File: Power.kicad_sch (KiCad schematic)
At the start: 6 parts, among them J3 Conn_01x02, Q1 Q_PMOS_GDS

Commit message: inital sch
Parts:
- removed R11: 49.9k, Resistor_SMD:R_0805_2012Metric, symbol Device:R_US
- added IC1: 1769205241, Active-PrechargeLib:1769205241, symbol DCDC-isolator:1769205241
- added ISO_PWR_TP1: TestPoint, utsvt-special:TestPoint_HEX_3mmID, symbol Connector:TestPoint
- added R1: 49.9k, Resistor_SMD:R_0805_2012Metric, symbol Device:R_US
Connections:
- net HVGND: now also IC1.4 (-VOUT)
- net ISO_PWR: now also IC1.5 (+VOUT), ISO_PWR_TP1.1
- net LV+: now also IC1.2 (+VIN)
- net LVGND: now also IC1.1 (-VIN), R1.1
- net at D1.2 (A), Q1.1 (G): now also R1.2
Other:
- removed sheet ActivePrecharge
- removed sheet CAN
- removed sheet ContactorDriver
- removed sheet PowerMisc
- moved on the sheet: 12V_TP1, D1, J3, LVGND_TP1, Q1

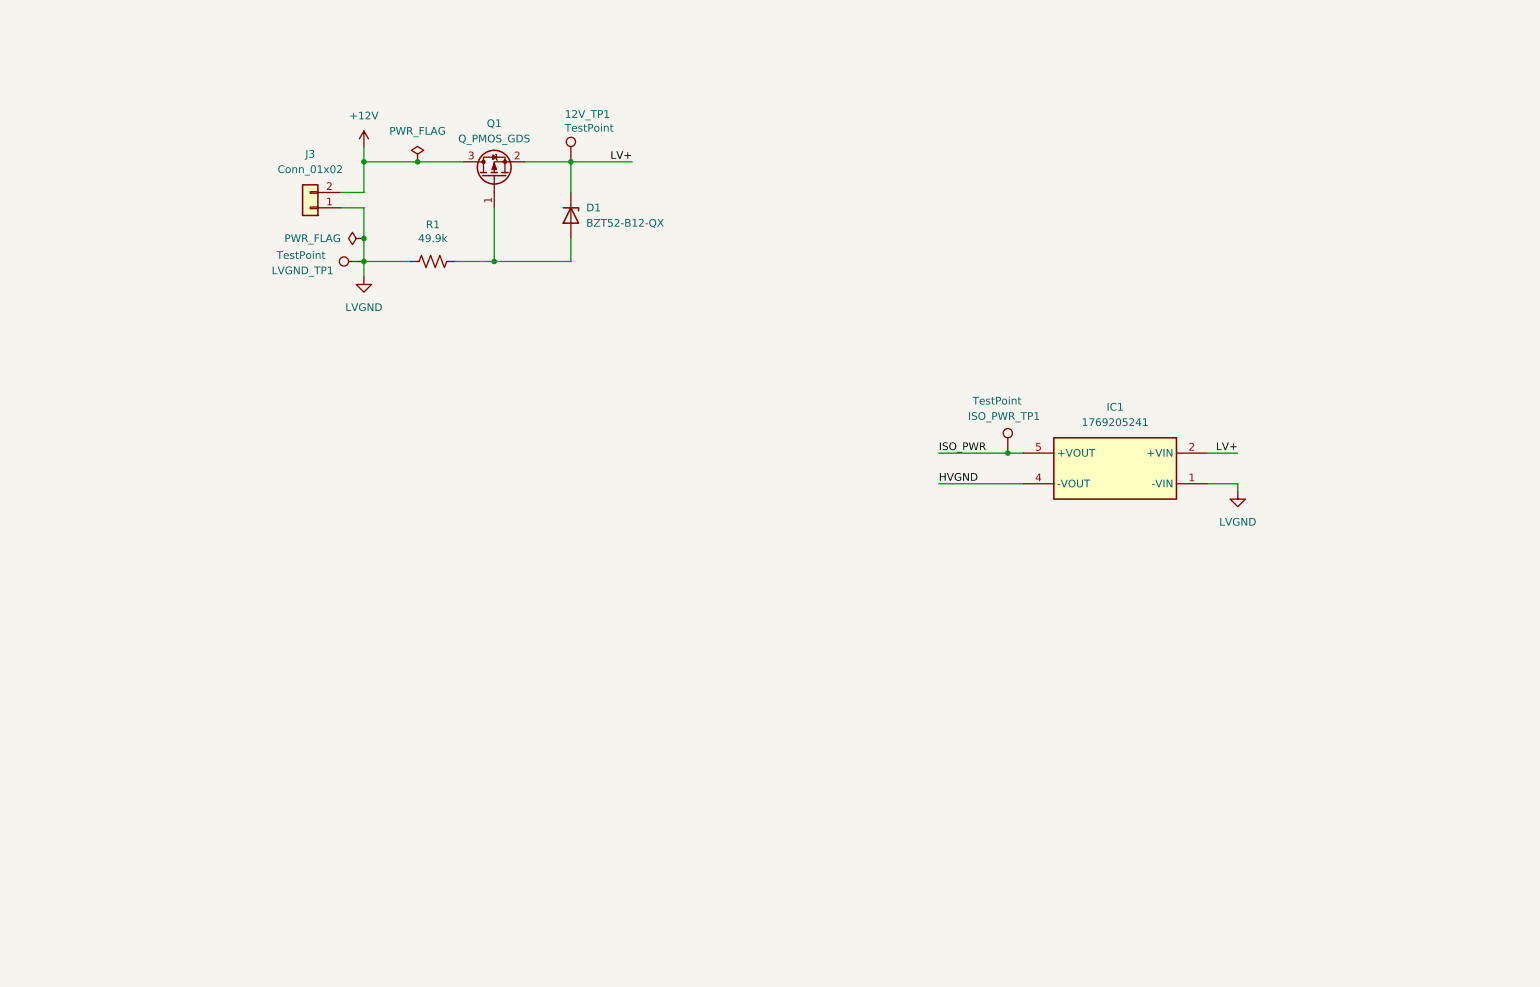
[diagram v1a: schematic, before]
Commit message: changed rpp ic
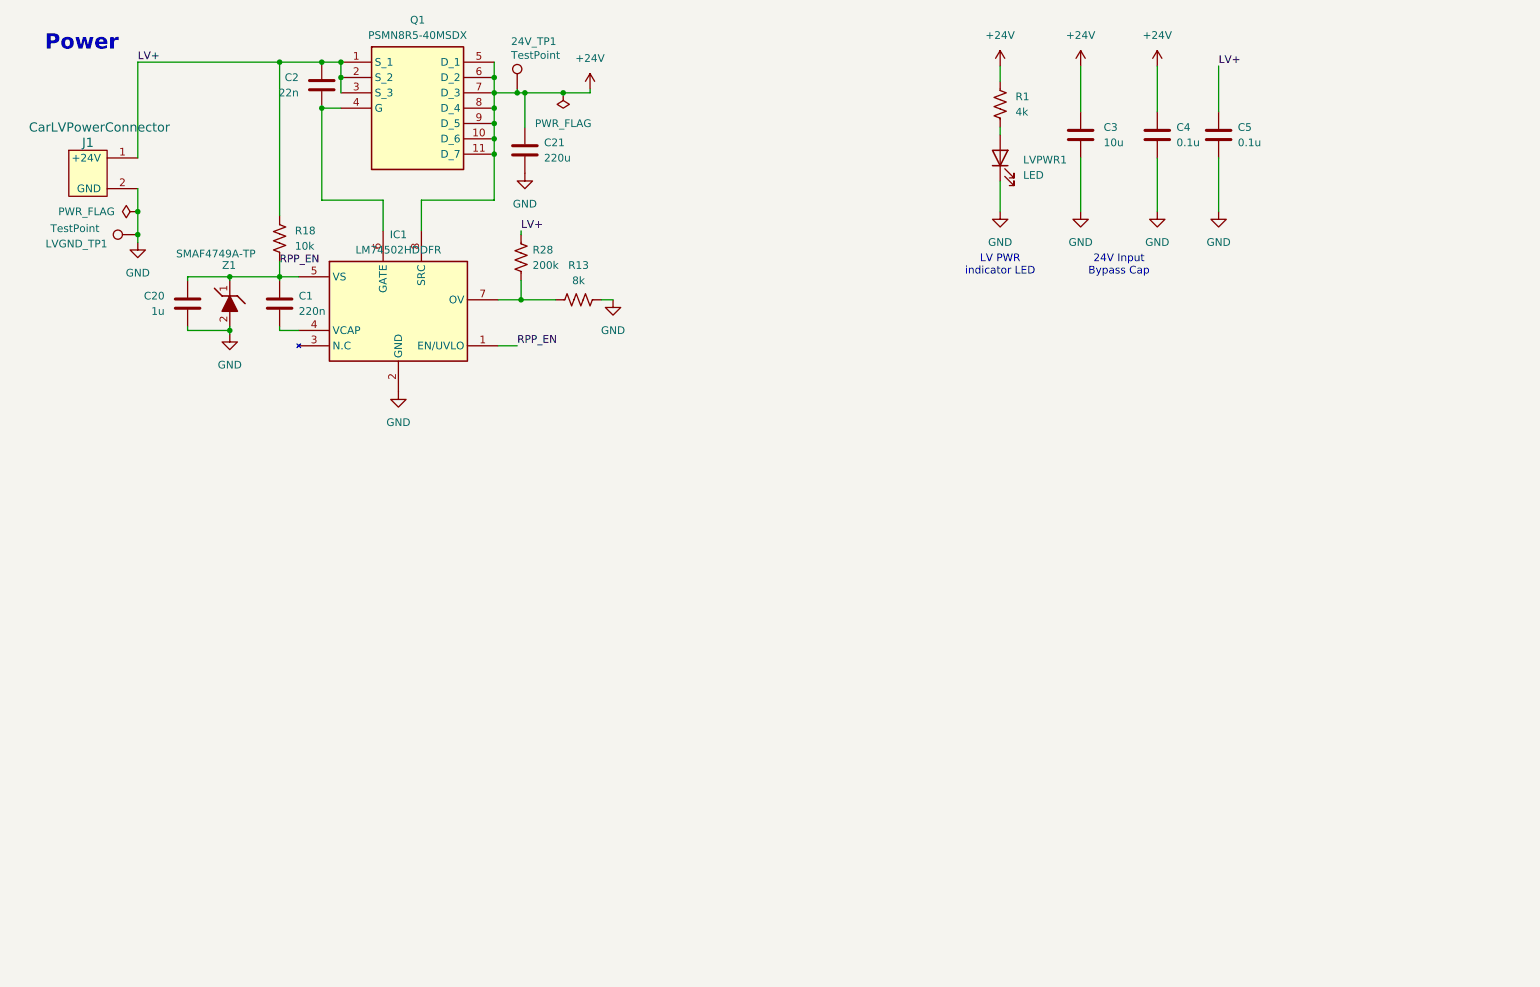
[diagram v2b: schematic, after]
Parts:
- removed D1: BZT52-B12-QX, Active-PrechargeLib:BZT52B12QX, symbol Device:D_Zener
- removed IC1: 1769205241, Active-PrechargeLib:1769205241, symbol DCDC-isolator:1769205241
- removed ISO_PWR_TP1: TestPoint, utsvt-special:TestPoint_HEX_3mmID, symbol Connector:TestPoint
- removed J3: Conn_01x02, utsvt-conn:Molex_MicroFit3.0_1x2xP3.00mm_PolarizingPeg_Vertical, symbol Connector_Generic:Conn_01x02
- removed Q1: Q_PMOS_GDS, Package_TO_SOT_SMD:SOT-23-3, symbol Device:Q_PMOS_GDS
- added C1: 220n, Capacitor_SMD:C_0603_1608Metric, symbol Device:C
- added C2: 22n, Capacitor_SMD:C_0603_1608Metric, symbol Device:C
- added C20: 1u, Capacitor_SMD:C_0603_1608Metric, symbol Device:C
- added C21: 220u, symbol Device:C
- added C3: 10u, Capacitor_SMD:C_0603_1608Metric, symbol Device:C
- added C4, C5: 0.1u, Capacitor_SMD:C_0603_1608Metric, symbol Device:C
- added IC1: LM74502HDDFR, SOT65P280X110-8N, symbol UTSVT_ICs:LM74502HDDFR
- added J1: CarLVPowerConnector, symbol UTSVT_Connectors:CarLVPowerConnector
- added LVPWR1: LED, LED_SMD:LED_0603_1608Metric, symbol Device:LED
- added Q1: PSMN8R5-40MSDX, PSMN8R5-40MSDX, symbol UTSVT_Power:PSMN8R5-40MSDX
- added R13: 8k, symbol Device:R_US
- added R18: 10k, symbol Device:R_US
- added R28: 200k, symbol Device:R_US
- added Z1: SMAF4749A-TP, SODFL5026X125N, symbol UTSVT_Power:SMAF4749A-TP
- 24V_TP1: renamed from 12V_TP1; footprint utsvt-special:TestPoint_HEX_3mmID -> UTSVT_Special:TestPoint_HEX_3mmID
- LVGND_TP1: footprint utsvt-special:TestPoint_HEX_3mmID -> UTSVT_Special:TestPoint_HEX_3mmID
- R1: value 49.9k -> 4k; footprint Resistor_SMD:R_0805_2012Metric -> Resistor_SMD:R_0603_1608Metric
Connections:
- net LV+: now also C2.2, C5.1, J1.1 (+24V), Q1.1 (S_1), Q1.2 (S_2), Q1.3 (S_3), R18.1, R28.1; no longer 24V_TP1.1
- net at R1.2: now also LVPWR1.2 (A)
- net LVGND renamed +24V
- net +24V: now also 24V_TP1.1, C21.1, C3.1, C4.1, IC1.8 (SRC), Q1.10 (D_6), Q1.11 (D_7), Q1.5 (D_1), Q1.6 (D_2), Q1.7 (D_3), Q1.8 (D_4), Q1.9 (D_5); no longer LVGND_TP1.1
- new net: C1.2, IC1.4 (VCAP)
- new net: C2.1, IC1.6 (GATE), Q1.4 (G)
- new net: IC1.7 (OV), R13.1, R28.2
- new net GND: C20.1, C21.2, C3.2, C4.2, C5.2, IC1.2 (GND), J1.2 (GND), LVGND_TP1.1, LVPWR1.1 (K), R13.2, Z1.2 (A)
- new net RPP_EN: C1.1, C20.2, IC1.1 (EN/UVLO), IC1.5 (VS), R18.2, Z1.1 (K)
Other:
- note added: "24V Input Bypass Cap"
- note added: "LV PWR indicator LED"
- note added: "Power"
- moved on the sheet: 24V_TP1, LVGND_TP1

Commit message: as;ldfkjasdl;f
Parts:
- added J3: Conn_01x02, UTSVT_Connectors:Molex_Nano-Fit_105309-xx02_1x02_P2.50mm_Vertical, symbol Connector_Generic:Conn_01x02
- C21: footprint (none) -> Capacitor_SMD:C_0603_1608Metric
- IC1: footprint SOT65P280X110-8N -> UTSVT_Power:SOT65P280X110-8N
- J1: footprint (none) -> UTSVT_Connectors:Molex_Nano-Fit_105309-xx02_1x02_P2.50mm_Vertical
- Q1: footprint PSMN8R5-40MSDX -> UTSVT_Power:PSMN8R5-40MSDX
- R13, R18, R28: footprint (none) -> Resistor_SMD:R_0603_1608Metric
- Z1: footprint SODFL5026X125N -> UTSVT_Passives:SODFL5026X125N
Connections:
- net GND: now also J3.1 (Pin_1)
- new net +3V3: J3.2 (Pin_2)
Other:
- note added: "3v3 injector"
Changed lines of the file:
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@@
 	(generator_version "9.0")
 	(paper "A4")
+	(text "3v3 injector"
+		(exclude_from_sim no)
+		(at 38.735 93.98 0)
+		(effects
+			(font
+				(size 1.27 1.27)
+			)
+		)
+	)
 	(text "LV PWR \nindicator LED"
 		(exclude_from_sim no)
@@
 	(wire
 		(pts
+			(xy 43.815 106.68) (xy 50.165 106.68)
+		)
+		(stroke
+			(width 0)
+			(type default)
+		)
+	)
+	(wire
+		(pts
 			(xy 106.68 33.02) (xy 106.68 35.56)
 		)
@@
 	(wire
 		(pts
+			(xy 43.815 104.14) (xy 50.165 104.14)
+		)
+		(stroke
+			(width 0)
+			(type default)
+		)
+	)
+	(wire
+		(pts
 			(xy 78.105 40.64) (xy 81.28 40.64)
 		)
@@
 	)
 	(symbol
+		(lib_id "power:GND")
+		(at 50.165 106.68 0)
+		(unit 1)
+		(exclude_from_sim no)
+		(in_bom yes)
+		(on_board yes)
+		(dnp no)
+		(fields_autoplaced yes)
+		(property "Reference" "#PWR045"
+			(at 50.165 113.03 0)
+			(effects
+				(font
+					(size 1.27 1.27)
+				)
+				(hide yes)
+			)
+		)
+		(property "Value" "GND"
+			(at 50.165 111.76 0)
+			(effects
+				(font
+					(size 1.27 1.27)
+				)
+			)
+		)
+		(property "Footprint" ""
+			(at 50.165 106.68 0)
+			(effects
+				(font
+					(size 1.27 1.27)
+				)
+				(hide yes)
+			)
+		)
+		(property "Datasheet" ""
+			(at 50.165 106.68 0)
+			(effects
+				(font
+					(size 1.27 1.27)
+				)
+				(hide yes)
+			)
+		)
+		(property "Description" "Power symbol creates a global label with name \"GND\" , ground"
+			(at 50.165 106.68 0)
+			(effects
+				(font
+					(size 1.27 1.27)
+				)
+				(hide yes)
+			)
+		)
+		(pin "1"
+		)
+		(instances
+			(project "VehicleControlUnit"
+				(path "/795c8e51-3ded-4d21-b864-aaff31c5def7/5469fc22-573e-4402-96df-d8b4b5bb4d29"
+					(reference "#PWR045")
+					(unit 1)
+				)
+			)
+		)
+	)
+	(symbol
 		(lib_id "power:+12V")
 		(at 216.535 33.655 0)
@@
 			)
 		)
-		(property "Footprint" ""
+		(property "Footprint" "Resistor_SMD:R_0603_1608Metric"
 			(at 72.136 62.484 90)
 			(effects
@@
 			)
 		)
-		(property "Footprint" "PSMN8R5-40MSDX"
+		(property "Footprint" "UTSVT_Power:PSMN8R5-40MSDX"
 			(at 102.87 127.94 0)
 			(effects
@@
 	)
 	(symbol
+		(lib_id "power:+3V3")
+		(at 50.165 104.14 0)
+		(unit 1)
+		(exclude_from_sim no)
+		(in_bom yes)
+		(on_board yes)
+		(dnp no)
+		(fields_autoplaced yes)
+		(property "Reference" "#PWR041"
+			(at 50.165 107.95 0)
+			(effects
+				(font
+					(size 1.27 1.27)
+				)
+				(hide yes)
+			)
+		)
+		(property "Value" "+3V3"
+			(at 50.165 99.06 0)
+			(effects
+				(font
+					(size 1.27 1.27)
+				)
+			)
+		)
+		(property "Footprint" ""
+			(at 50.165 104.14 0)
+			(effects
+				(font
+					(size 1.27 1.27)
+				)
+				(hide yes)
+			)
+		)
+		(property "Datasheet" ""
+			(at 50.165 104.14 0)
+			(effects
+				(font
+					(size 1.27 1.27)
+				)
+				(hide yes)
+			)
+		)
+		(property "Description" "Power symbol creates a global label with name \"+3V3\""
+			(at 50.165 104.14 0)
+			(effects
+				(font
+					(size 1.27 1.27)
+				)
+				(hide yes)
+			)
+		)
+		(pin "1"
+		)
+		(instances
+			(project "VehicleControlUnit"
+				(path "/795c8e51-3ded-4d21-b864-aaff31c5def7/5469fc22-573e-4402-96df-d8b4b5bb4d29"
+					(reference "#PWR041")
+					(unit 1)
+				)
+			)
+		)
+	)
+	(symbol
 		(lib_id "power:GND")
 		(at 203.835 57.785 0)
@@
 	)
 	(symbol
+		(lib_id "Connector_Generic:Conn_01x02")
+		(at 38.735 106.68 180)
+		(unit 1)
+		(exclude_from_sim no)
+		(in_bom yes)
+		(on_board yes)
+		(dnp no)
+		(fields_autoplaced yes)
+		(property "Reference" "J3"
+			(at 38.735 97.79 0)
+			(effects
+				(font
+					(size 1.27 1.27)
+				)
+			)
+		)
+		(property "Value" "Conn_01x02"
+			(at 38.735 100.33 0)
+			(effects
+				(font
+					(size 1.27 1.27)
+				)
+			)
+		)
+		(property "Footprint" "UTSVT_Connectors:Molex_Nano-Fit_105309-xx02_1x02_P2.50mm_Vertical"
+			(at 38.735 106.68 0)
+			(effects
+				(font
+					(size 1.27 1.27)
+				)
+				(hide yes)
+			)
+		)
+		(property "Datasheet" "~"
+			(at 38.735 106.68 0)
+			(effects
+				(font
+					(size 1.27 1.27)
+				)
+				(hide yes)
+			)
+		)
+		(property "Description" "Generic connector, single row, 01x02, script generated (kicad-library-utils/schlib/autogen/connector/)"
+			(at 38.735 106.68 0)
+			(effects
+				(font
+					(size 1.27 1.27)
+				)
+				(hide yes)
+			)
+		)
+		(pin "2"
+		)
+		(pin "1"
+		)
+		(instances
+			(project ""
+				(path "/795c8e51-3ded-4d21-b864-aaff31c5def7/5469fc22-573e-4402-96df-d8b4b5bb4d29"
+					(reference "J3")
+					(unit 1)
+				)
+			)
+		)
+	)
+	(symbol
 		(lib_id "UTSVT_ICs:LM74502HDDFR")
 		(at 74.295 68.58 0)
@@
 			)
 		)
-		(property "Footprint" "SOT65P280X110-8N"
+		(property "Footprint" "UTSVT_Power:SOT65P280X110-8N"
 			(at 103.505 163.5 0)
 			(effects
@@
 			)
 		)
-		(property "Footprint" "SODFL5026X125N"
+		(property "Footprint" "UTSVT_Passives:SODFL5026X125N"
 			(at -30.785 76.835 0)
 			(effects
@@
 			)
 		)
-		(property "Footprint" ""
+		(property "Footprint" "Capacitor_SMD:C_0603_1608Metric"
 			(at 112.7252 51.435 0)
 			(effects
@@
 			)
 		)
-		(property "Footprint" ""
+		(property "Footprint" "Resistor_SMD:R_0603_1608Metric"
 			(at 120.904 71.374 90)
 			(effects
@@
 			)
 		)
-		(property "Footprint" ""
+		(property "Footprint" "Resistor_SMD:R_0603_1608Metric"
 			(at 112.141 65.659 90)
 			(effects
@@
 			)
 		)
-		(property "Footprint" ""
+		(property "Footprint" "UTSVT_Connectors:Molex_Nano-Fit_105309-xx02_1x02_P2.50mm_Vertical"
 			(at 40.005 51.435 0)
 			(effects

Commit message: maybe final revA revision
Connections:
- net +3V3 renamed 3V3_LSOM

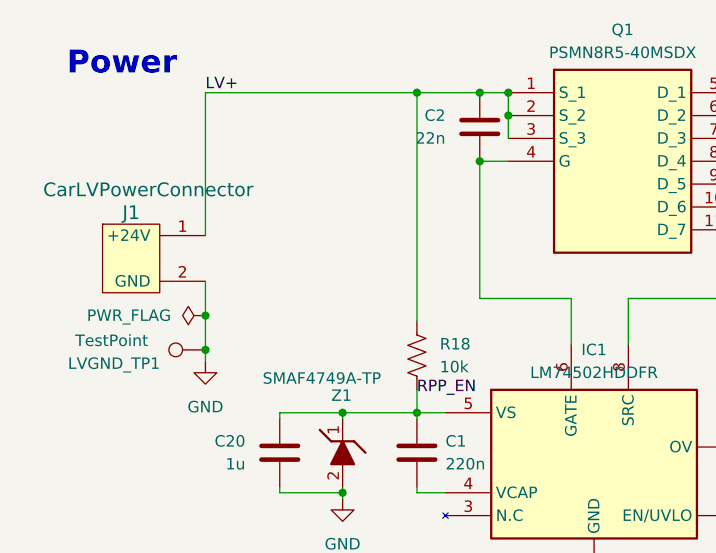
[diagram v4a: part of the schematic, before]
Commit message: small zener diode change
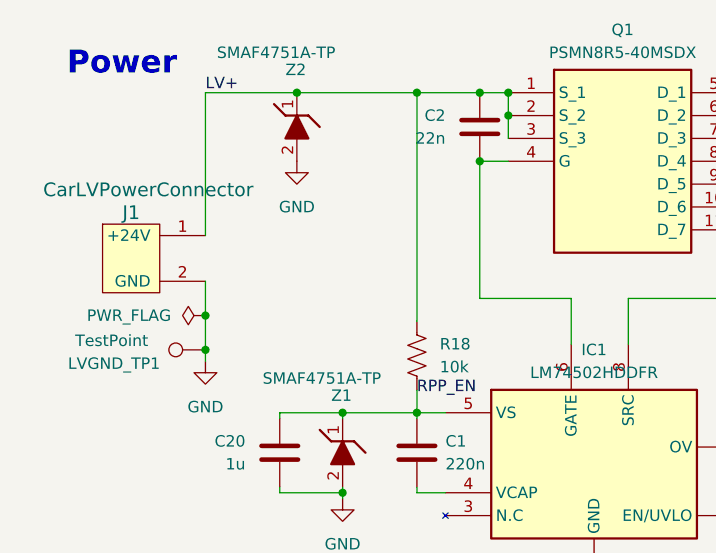
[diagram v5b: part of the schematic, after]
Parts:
- added Z2: SMAF4751A-TP, UTSVT_Passives:SODFL5026X125N, symbol UTSVT_Power:SMAF4749A-TP
- Z1: value SMAF4749A-TP -> SMAF4751A-TP
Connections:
- net GND: now also Z2.2 (A)
- net LV+: now also Z2.1 (K)
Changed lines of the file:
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@@
 	)
 	(junction
+		(at 57.785 33.02)
+		(diameter 0)
+		(color 0 0 0 0)
+	)
+	(junction
 		(at 62.865 77.47)
 		(diameter 0)
@@
 	(wire
 		(pts
-			(xy 47.625 33.02) (xy 71.12 33.02)
+			(xy 47.625 33.02) (xy 57.785 33.02)
 		)
 		(stroke
@@
 	(wire
 		(pts
+			(xy 57.785 33.02) (xy 71.12 33.02)
+		)
+		(stroke
+			(width 0)
+			(type default)
+		)
+	)
+	(wire
+		(pts
 			(xy 111.76 38.1) (xy 118.11 38.1)
 		)
@@
 	(symbol
 		(lib_id "UTSVT_Power:SMAF4749A-TP")
+		(at 57.785 30.48 270)
+		(unit 1)
+		(exclude_from_sim no)
+		(in_bom yes)
+		(on_board yes)
+		(dnp no)
+		(property "Reference" "Z2"
+			(at 56.515 30.48 90)
+			(effects
+				(font
+					(size 1.27 1.27)
+				)
+				(justify left)
+			)
+		)
+		(property "Value" "SMAF4751A-TP"
+			(at 48.895 28.575 90)
+			(effects
+				(font
+					(size 1.27 1.27)
+				)
+				(justify left)
+			)
+		)
+		(property "Footprint" "UTSVT_Passives:SODFL5026X125N"
+			(at -35.865 40.64 0)
+			(effects
+				(font
+					(size 1.27 1.27)
+				)
+				(justify left top)
+				(hide yes)
+			)
+		)
+		(property "Datasheet" "https://www.mccsemi.com/pdf/Products/SMAF4735A_SMAF4764A(DO-221AC).pdf"
+			(at -135.865 40.64 0)
+			(effects
+				(font
+					(size 1.27 1.27)
+				)
+				(justify left top)
+				(hide yes)
+			)
+		)
+		(property "Description" "1.0 Watt Zener Diodes 6.2V to 100V"
+			(at 57.785 30.48 0)
+			(effects
+				(font
+					(size 1.27 1.27)
+				)
+				(hide yes)
+			)
+		)
+		(property "Height" "1.25"
+			(at -335.865 40.64 0)
+			(effects
+				(font
+					(size 1.27 1.27)
+				)
+				(justify left top)
+				(hide yes)
+			)
+		)
+		(property "Mouser Part Number" "833-SMAF4749A-TP"
+			(at -435.865 40.64 0)
+			(effects
+				(font
+					(size 1.27 1.27)
+				)
+				(justify left top)
+				(hide yes)
+			)
+		)
+		(property "Mouser Price/Stock" "https://www.mouser.co.uk/ProductDetail/Micro-Commercial-Components-MCC/SMAF4749A-TP?qs=%252BXxaIXUDbq1bdSZ3Ebik%2FA%3D%3D"
+			(at -535.865 40.64 0)
+			(effects
+				(font
+					(size 1.27 1.27)
+				)
+				(justify left top)
+				(hide yes)
+			)
+		)
+		(property "Manufacturer_Name" "MCC"
+			(at -635.865 40.64 0)
+			(effects
+				(font
+					(size 1.27 1.27)
+				)
+				(justify left top)
+				(hide yes)
+			)
+		)
+		(property "Manufacturer_Part_Number" "SMAF4749A-TP"
+			(at -735.865 40.64 0)
+			(effects
+				(font
+					(size 1.27 1.27)
+				)
+				(justify left top)
+				(hide yes)
+			)
+		)
+		(pin "1"
+		)
+		(pin "2"
+		)
+		(instances
+			(project "VehicleControlUnit"
+				(path "/795c8e51-3ded-4d21-b864-aaff31c5def7/5469fc22-573e-4402-96df-d8b4b5bb4d29"
+					(reference "Z2")
+					(unit 1)
+				)
+			)
+		)
+	)
+	(symbol
+		(lib_id "UTSVT_Power:SMAF4749A-TP")
 		(at 62.865 66.675 270)
 		(unit 1)
@@
 			)
 		)
-		(property "Value" "SMAF4749A-TP"
+		(property "Value" "SMAF4751A-TP"
 			(at 53.975 64.77 90)
 			(effects
@@
 					(unit 1)
 				)
+			)
+		)
+	)
+	(symbol
+		(lib_id "power:GND")
+		(at 57.785 40.64 0)
+		(unit 1)
+		(exclude_from_sim no)
+		(in_bom yes)
+		(on_board yes)
+		(dnp no)
+		(fields_autoplaced yes)
+		(property "Reference" "#PWR076"
+			(at 57.785 46.99 0)
+			(effects
+				(font
+					(size 1.27 1.27)
+				)
+				(hide yes)
+			)
+		)
+		(property "Value" "GND"
+			(at 57.785 45.72 0)
+			(effects
+				(font
+					(size 1.27 1.27)
+				)
+			)
+		)
+		(property "Footprint" ""
+			(at 57.785 40.64 0)
+			(effects
+				(font
+					(size 1.27 1.27)
+				)
+				(hide yes)
+			)
+		)
+		(property "Datasheet" ""
+			(at 57.785 40.64 0)
+			(effects
+				(font
+					(size 1.27 1.27)
+				)
+				(hide yes)
+			)
+		)
+		(property "Description" "Power symbol creates a global label with name \"GND\" , ground"
+			(at 57.785 40.64 0)
+			(effects
+				(font
+					(size 1.27 1.27)
+				)
+				(hide yes)
+			)
+		)
+		(pin "1"
+		)
+		(instances
+			(project "VehicleControlUnit"
+				(path "/795c8e51-3ded-4d21-b864-aaff31c5def7/5469fc22-573e-4402-96df-d8b4b5bb4d29"
+					(reference "#PWR076")
+					(unit 1)
+				)

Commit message: lakshay edits
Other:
- moved on the sheet: R18
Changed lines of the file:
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@@
 	(wire
 		(pts
-			(xy 71.12 58.42) (xy 71.12 33.02)
+			(xy 71.12 55.245) (xy 71.12 33.02)
 		)
 		(stroke
@@
 	(wire
 		(pts
-			(xy 71.12 66.04) (xy 71.12 68.58)
+			(xy 71.12 62.865) (xy 71.12 68.58)
 		)
 		(stroke
@@
 	(symbol
 		(lib_id "Device:R_US")
-		(at 71.12 62.23 0)
+		(at 71.12 59.055 0)
 		(unit 1)
 		(exclude_from_sim no)
@@
 		(fields_autoplaced yes)
 		(property "Reference" "R18"
-			(at 73.66 60.9599 0)
+			(at 73.66 57.7849 0)
 			(effects
 				(font
@@
 		)
 		(property "Value" "10k"
-			(at 73.66 63.4999 0)
+			(at 73.66 60.3249 0)
 			(effects
 				(font
@@
 		)
 		(property "Footprint" "Resistor_SMD:R_0603_1608Metric"
-			(at 72.136 62.484 90)
+			(at 72.136 59.309 90)
 			(effects
 				(font
@@
 		)
 		(property "Datasheet" "~"
-			(at 71.12 62.23 0)
+			(at 71.12 59.055 0)
 			(effects
 				(font
@@
 		)
 		(property "Description" "Resistor, US symbol"
-			(at 71.12 62.23 0)
-			(effects
-				(font
+			(at 71.12 59.055 0)
+			(effects
+				(font
